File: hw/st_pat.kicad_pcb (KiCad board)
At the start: 2 copper layers, 17 parts, among them J3 SHARP Display, J4 BATTERY, J5 Compass Right, J6 Compass Left, SW1 SW_PWR, SW2 BTN_RST, SW3 BTN, SW4 BTN, SW5 BTN, U1 FGPMMOPA6H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

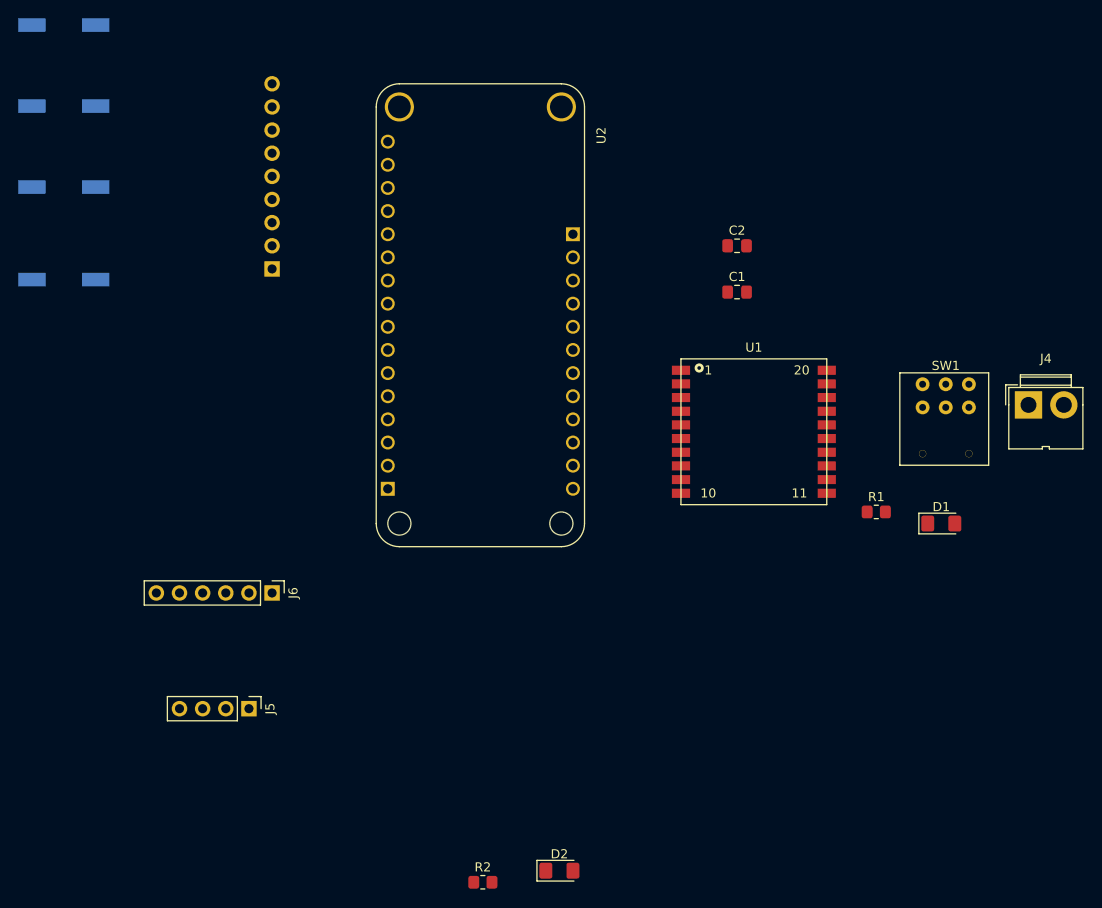
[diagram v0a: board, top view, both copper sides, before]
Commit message: Add one more led to schematic and create pcb
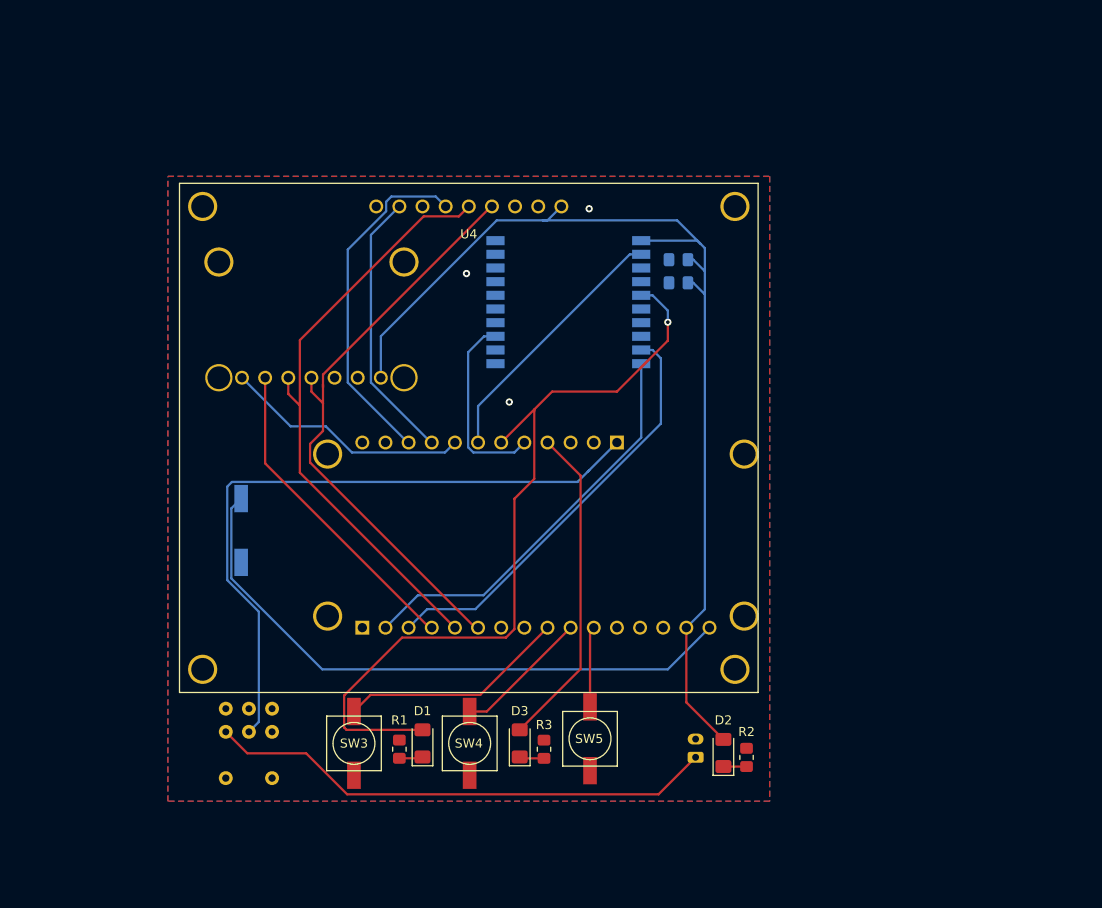
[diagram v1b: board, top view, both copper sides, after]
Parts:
- removed J3: SHARP Display, Connector_PinHeader_2.54mm:PinHeader_1x09_P2.54mm_Vertical
- removed J5: Compass Right, Connector_PinHeader_2.54mm:PinHeader_1x04_P2.54mm_Vertical
- removed J6: Compass Left, Connector_PinHeader_2.54mm:PinHeader_1x06_P2.54mm_Vertical
- added D3: GEN_BLU, LED_SMD:LED_1206_3216Metric_Pad1.42x1.75mm_HandSolder, F.Cu at (145.3, 114.3)
- added R3: 100, Resistor_SMD:R_0805_2012Metric_Pad1.20x1.40mm_HandSolder, F.Cu at (148.0, 114.9)
- added U3: LIS2MDL_ADAFRUIT, st_pat:LIS3MDL_ADAFRUIT, B.Cu at (127.5, 56.4)
- added U4: Sharp_Display, st_pat:Sharp_Display, F.Cu at (149.9, 55.4)
- C1, C2: moved to B.Cu
- J4: footprint Connector:JWT_A3963_1x02_P3.96mm_Vertical -> Connector_JST:JST_PH_S2B-PH-K_1x02_P2.00mm_Horizontal; moved to B.Cu
- SW1: footprint st_pats:SW_Rocker_A22K1H-EA -> st_pat:SW_Rocker_A22K1H-EA; moved to B.Cu
- SW2: footprint st_pats:SW_Mini_Soft -> st_pat:SW_Mini_Soft
- SW3, SW4, SW5: footprint st_pats:SW_Mini_Soft -> st_pat:SW_Mini_Soft; moved to F.Cu
- U1: footprint st_pats:FGPMMOPA6H -> st_pat:FGPMMOPA6H; moved to B.Cu
- U2: footprint st_pats:MODULE_FEATHER_M0_BASIC_PROTO -> FEATHER_M0_BASIC_PROTO:FEATHER_M0_BASIC_PROTO; moved to B.Cu
- moved SW3 84.9 mm to (127.0, 114.3), turned to 270 degrees
- moved SW5 83.5 mm to (152.9, 113.8), turned to 270 degrees
- moved SW4 82.8 mm to (139.7, 114.3), turned to 270 degrees
- moved SW1 79.8 mm to (118.1, 110.5), turned to 180 degrees
- moved D1 61.8 mm to (134.6, 114.3), turned to 90 degrees
- moved R1 58.5 mm to (132.1, 114.9), turned to 90 degrees
- moved J4 53.2 mm to (164.6, 115.8), turned to 90 degrees
- moved SW2 33.7 mm to (114.8, 90.9), turned to 270 degrees
- moved R2 32.0 mm to (170.2, 115.8), turned to 90 degrees
- moved U2 24.9 mm to (147.1, 91.4), turned to 180 degrees
- moved U1 24.8 mm to (150.6, 55.6), turned to 180 degrees
- moved D2 22.2 mm to (167.6, 115.4), turned to 90 degrees
- moved C2 6.61 mm to (162.7, 61.2), turned to 180 degrees
- moved C1 6.51 mm to (162.7, 63.8), turned to 180 degrees
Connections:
- R2 pad 1: GND -> Net-(D2-Pad1)
- R2 pad 2: Net-(D2-Pad1) -> GND
- SW1 pad 1: Net-(SW1-Pad1) -> (no net)
- SW1 pad 2: Net-(SW1-Pad2) -> (no net)
- SW1 pad 3: Net-(SW1-Pad3) -> (no net)
- SW1 pad 4: Net-(SW1-Pad4) -> (no net)
- U1 pad 11: Net-(U1-Pad11) -> (no net)
- U1 pad 14: Net-(U1-Pad14) -> (no net)
- U1 pad 15: Net-(U1-Pad15) -> (no net)
- U1 pad 16: Net-(U1-Pad16) -> (no net)
- U1 pad 17: Net-(U1-Pad17) -> (no net)
- U1 pad 18: Net-(U1-Pad18) -> (no net)
- U1 pad 20: Net-(U1-Pad20) -> (no net)
- U1 pad 4: Net-(U1-Pad4) -> (no net)
- U1 pad 6: Net-(U1-Pad6) -> (no net)
- U1 pad 7: Net-(U1-Pad7) -> (no net)
- U2 pad P1_12: Net-(U2-PadP1_12) -> (no net)
- U2 pad P1_14: Net-(U2-PadP1_14) -> (no net)
- U2 pad P1_7: /CPS_RDY_A5 -> (no net)
- U2 pad P1_8: /CPS_CS_A4 -> (no net)
- U2 pad P2_11: Net-(U2-PadP2_11) -> (no net)
- U2 pad P2_12: Net-(U2-PadP2_12) -> (no net)
- U2 pad P2_2: Net-(U2-PadP2_2) -> (no net)
- U2 pad P2_3: Net-(U2-PadP2_3) -> (no net)
- U2 pad P2_8: Net-(U2-PadP2_8) -> /CPS_CS_D9
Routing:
- net +3V3: track 0.00 -> 118.1 mm
- net /GPS_FIX_D11: track 0.00 -> 89.3 mm, vias 0 -> 1
- net +BATT: track 0.00 -> 73.8 mm
- net /RST: track 0.00 -> 67.7 mm
- net /MOSI: track 0.00 -> 66.8 mm
- net /SCK: track 0.00 -> 66.4 mm
- net Net-(J4-Pad1): track 0.00 -> 56.1 mm
- net /RX: track 0.00 -> 46.7 mm
- net /TX: track 0.00 -> 44.8 mm
- net /SHARP_CS_D5: track 0.00 -> 38.2 mm
- net Net-(D3-Pad2): track 0.00 -> 35.8 mm
- net /MISO: track 0.00 -> 35.2 mm
- net /SHARP_DISP_D6: track 0.00 -> 30.0 mm
- net /GPS_RST_D10: track 0.00 -> 28.8 mm
- net /CPS_CS_D9: track 0.00 -> 27.2 mm
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- added copper zone on B.Cu, net GND
- added copper zone on F.Cu, net GND
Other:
- board text removed: "Not sure if this is the right battery connector"
